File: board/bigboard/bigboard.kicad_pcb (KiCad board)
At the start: 4 copper layers, 89.9 x 88.8 mm, 143 parts, among them J1 Conn_02x02_Row_Letter_First, J10 Conn_02x03_Row_Letter_First, J11 Conn_01x02_Male, J12 Conn_01x03_Male, J13 Conn_02x07_Row_Letter_First, J2 Conn_02x02_Row_Letter_First, J3 USB_C_Receptacle_USB2.0, J4 Conn_01x03_Male, J5 Conn_01x03_Male, J6 Conn_01x03_Male, J7 Conn_01x03_Male, J8 Conn_2Rows-21Pins_MountingPin, J9 Conn_01x05_Male, M1 Motor_AC, Q1 Q_Dual_PMOS_G1S2G2D2S1D1, SW1 SW_Push, SW2 SW_Push, SW3 SW_Push, SW4 SW_Push, SW5 SW_Push, SW6 SW_Push, SW7 SW_Push, SW8 SW_Push, U1 BQ51221YFPT, U10 APDS-9306-065, U11 TXB0104D, U12 PCF85263AT/AJ, U2 MAX20353AEWN+, U3 D52MxxM8, U4 RP2040, U5 SN74LXCH8T245PWR, U6 SN74LXCH8T245PWR, U7 GD25LQ128DSIGR, U8 BMM150, U9 BMI270, Y1 12MHz, Y2 32.768kHz

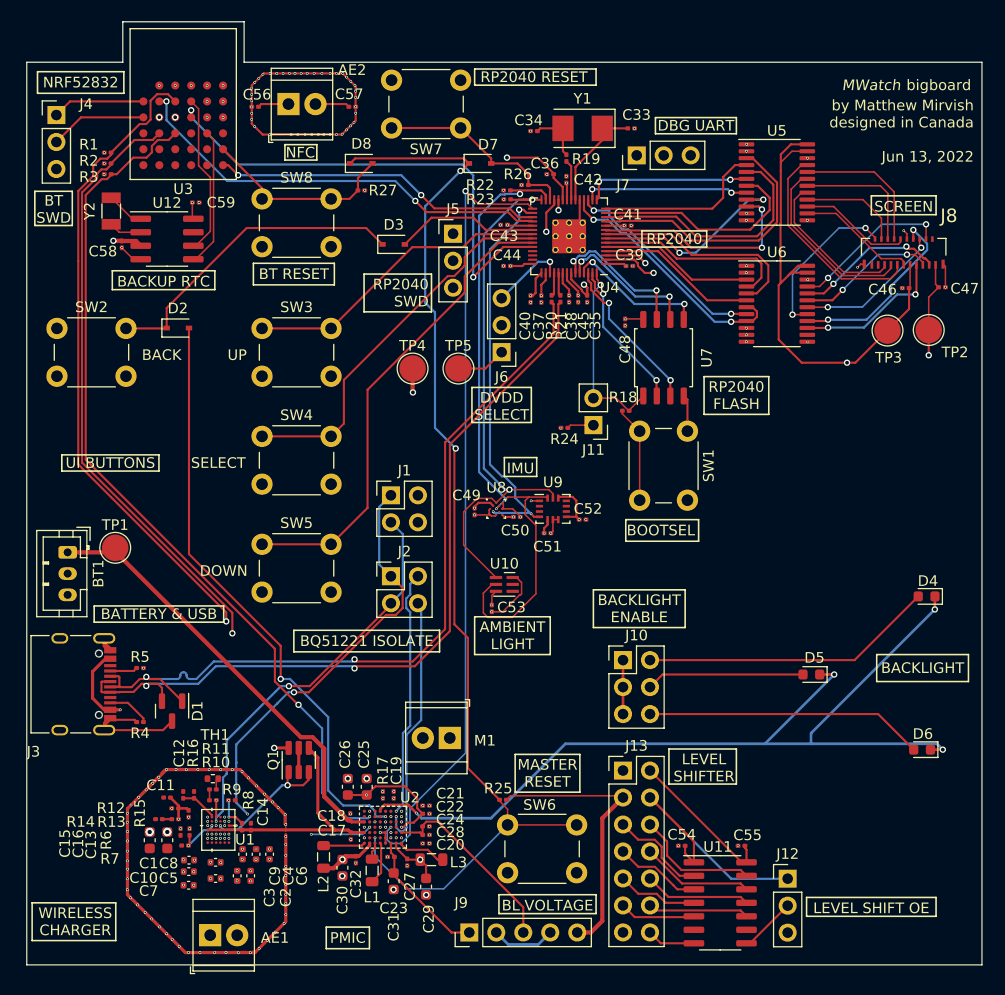
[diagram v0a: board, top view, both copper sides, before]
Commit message: Manufactured version of bigboard
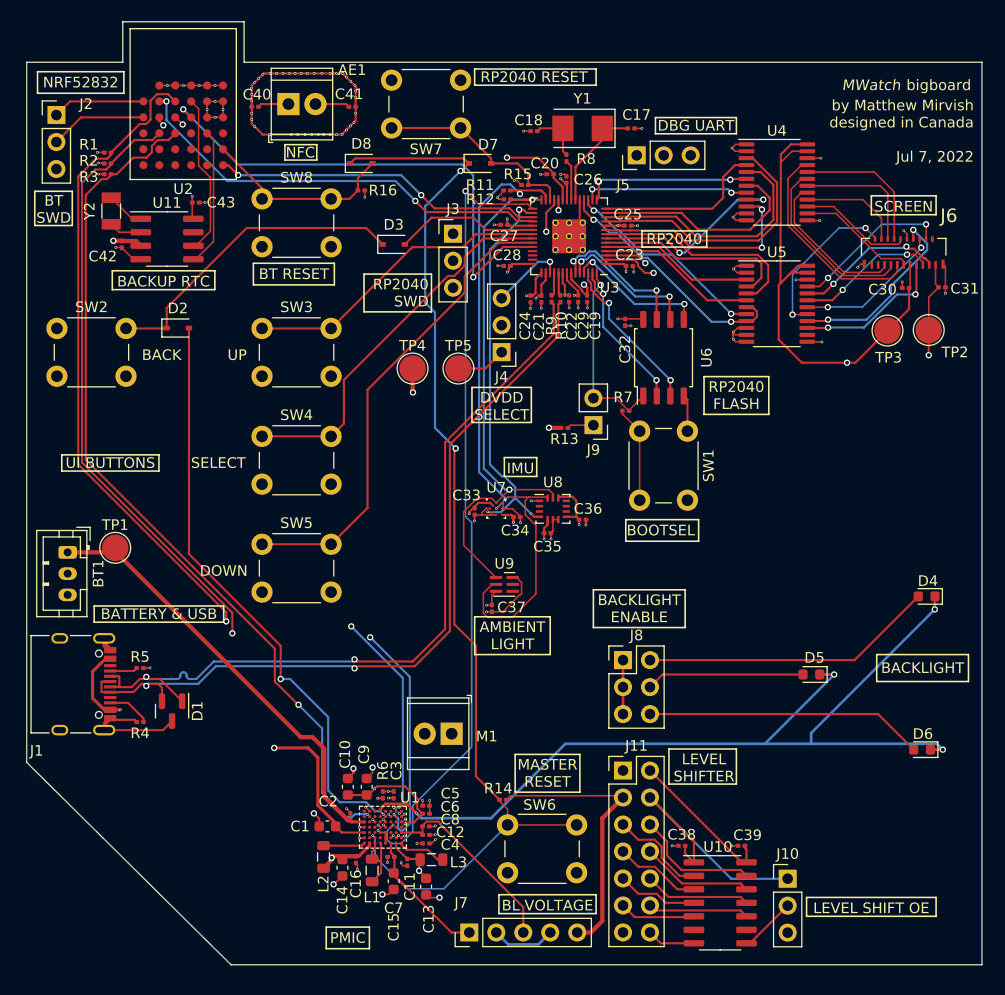
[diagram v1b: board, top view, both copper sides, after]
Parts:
- removed the AE1 at (115.3, 143.8)
- removed the C1 at (113.3, 136.7)
- removed the C10 at (113.3, 137.8)
- removed the C11 at (111.3, 130.8)
- removed the C12 at (112.8, 130.6)
- removed the C13 at (112.5, 134.1)
- removed the C14 at (119.2, 133.6)
- removed the C15 at (109.6, 134.8)
- removed the C16 at (111.3, 134.8)
- removed the C2 at (119.1, 138.2)
- removed the C3 at (117.9, 138.2)
- removed the C4 at (119.6, 136.1)
- removed the C5 at (115.8, 138.4)
- removed the C6 at (120.9, 136.1)
- removed the C7 at (113.3, 139.1)
- removed the C8 at (115.8, 136.9)
- removed the C9 at (118.4, 136.1)
- removed the J1 at (132.3, 102.4)
- removed the J2 at (132.3, 110.0)
- removed Q1: Q_Dual_PMOS_G1S2G2D2S1D1, Package_TO_SOT_SMD:SOT-23-6
- removed the R10 at (115.6, 131.1)
- removed the R11 at (115.6, 130.0)
- removed the R12 at (112.0, 131.8)
- removed the R13 at (112.0, 132.8)
- removed the R14 at (110.5, 132.8)
- removed the R15 at (113.3, 132.3)
- removed the R16 at (113.8, 130.6)
- removed the R6 at (113.4, 134.1)
- removed the R7 at (112.9, 135.3)
- removed the R8 at (118.3, 133.6)
- removed the R9 at (117.3, 131.1)
- removed TH1: NTCG103JF103FT1, Resistor_SMD:R_0402_1005Metric
- removed the U1 at (116.1, 133.8)
- C1: renamed from C17; footprint Capacitor_SMD:C_0201_0603Metric -> Capacitor_SMD:C_0603_1608Metric
- D1: value SP0502BAHT -> SP0502BAHTG
- R6: renamed from R17; value 4k -> 4.02k
- U4: renamed from U5; value SN74LXCH8T245PWR -> SN74LVC8T245PWR
- U5: renamed from U6; value SN74LXCH8T245PWR -> SN74LVC8T245PWR
- moved C1 2.38 mm to (126.3, 133.5), turned to 180 degrees
- moved M1 0.44 mm to (138.0, 124.8)
- renumbered AE2 to AE1, C26 to C10, C27 to C11, C28 to C12, C29 to C13, C30 to C14, C31 to C15, C32 to C16, C33 to C17, C34 to C18, C35 to C19, C18 to C2, C36 to C20, C37 to C21, C38 to C22, C39 to C23, C40 to C24, C41 to C25, C42 to C26, C43 to C27, C44 to C28, C45 to C29, C19 to C3, C46 to C30, C47 to C31, C48 to C32, C49 to C33, C50 to C34, C51 to C35, C52 to C36, C53 to C37, C54 to C38, C55 to C39, C20 to C4, C56 to C40, C57 to C41, C58 to C42, C59 to C43, C21 to C5, C22 to C6, C23 to C7, C24 to C8, C25 to C9, J3 to J1, J12 to J10, J13 to J11, J4 to J2, J5 to J3, J6 to J4, J7 to J5, J8 to J6, J9 to J7, J10 to J8, J11 to J9, R21 to R10, R22 to R11, R23 to R12, R24 to R13, R25 to R14, R26 to R15, R27 to R16, R18 to R7, R19 to R8, R20 to R9, U2 to U1, U11 to U10, U12 to U11, U3 to U2, U4 to U3, U7 to U6, U8 to U7, U9 to U8, U10 to U9
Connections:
- C1 pad 1: /Power/WirelessPower/OUT -> /Power/PMIC/VCHG_IN
- J1 pad A4: /Power/USB/VBUS_OUT -> /Power/PMIC/VCHG_IN
- J1 pad A9: /Power/USB/VBUS_OUT -> /Power/PMIC/VCHG_IN
- J1 pad B4: /Power/USB/VBUS_OUT -> /Power/PMIC/VCHG_IN
- J1 pad B9: /Power/USB/VBUS_OUT -> /Power/PMIC/VCHG_IN
- U1 pad C5: /Power/PMIC/EOC_CTRL -> unconnected-(U1-PadC5)
- U1 pad G4: /Power/PMIC/PD_DET -> unconnected-(U1-PadG4)
- U1 pad H5: /Power/WirelessPower/OUT -> /Power/PMIC/VCHG_IN
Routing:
- net /Power/WirelessPower/SCL_POWER: track 44.1 -> 0.00 mm, vias 3 -> 0
- net /Power/PMIC/VCHG_IN: track 0.00 -> 38.5 mm, vias 0 -> 2
- net /Power/WirelessPower/SDA_POWER: track 37.5 -> 0.00 mm, vias 2 -> 0
- net /Power/USB/VBUS_OUT: track 34.8 -> 0.00 mm, vias 3 -> 0
- net +1V8: track 88.4 -> 115.0 mm, vias 32 -> 29
- net /Power/WirelessPower/OUT: track 24.0 -> 0.00 mm
- net /Power/PMIC/EOC_CTRL: track 23.3 -> 0.00 mm, vias 2 -> 0
- net /Power/PMIC/PD_DET: track 16.5 -> 0.00 mm, vias 3 -> 0
- net Net-(Q1-Pad1): track 12.8 -> 0.00 mm, vias 2 -> 0
- net /BT/SCL_POWER: track 104.3 -> 93.6 mm, vias 2 -> 3
- net /Power/WirelessPower/RECT: track 8.61 -> 0.00 mm, vias 9 -> 0
- net /Power/WirelessPower/AC_COIL2: track 8.59 -> 0.00 mm, vias 8 -> 0
- net /Power/WirelessPower/FOD: track 8.34 -> 0.00 mm, vias 2 -> 0
- net Net-(C7-Pad1): track 7.72 -> 0.00 mm, vias 2 -> 0
- net /BT/SDA_POWER: track 100.0 -> 93.0 mm, vias 2 -> 3
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- removed copper zone on In1.Cu, net /Power/WirelessPower/AC1
- removed copper zone on In1.Cu, net /Power/WirelessPower/AC_COIL1
- removed copper zone on In1.Cu, net /Power/WirelessPower/AC_COIL2
- removed copper zone on In2.Cu, net /Power/WirelessPower/RECT
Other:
- outline, holes or cut-outs redrawn
- board text added: "by Matthew Mirvish designed in Canada Jul 7, 2022"
- board text removed: "BQ51221 ISOLATE"
- board text removed: "WIRELESS CHARGER"
- board text removed: "by Matthew Mirvish designed in Canada Jun 13, 2022"

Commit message: Update board to kicad 7
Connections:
- net /LCD/LCD.VCOM renamed /LCD/LCD.VB
- net Net-(J2-Pad1) renamed /BT/BT_SWDIO
- net Net-(J2-Pad2) renamed /BT/BT_SWCLK
- net Net-(J3-Pad1) renamed /RP2040/RP_SWCLK
- net Net-(J3-Pad2) renamed /RP2040/RP_SWDIO
